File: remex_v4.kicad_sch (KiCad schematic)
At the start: 22 parts, among them J1 Conn_01x03_Male, J10 Conn_01x04_Male, J11 Conn_01x04_Male, J2 Conn_01x03_Male, J3 Conn_01x06_Male, J4 Conn_01x04_Male, J5 Conn_01x02_Male, J6 Conn_01x03_Male, J7 Conn_01x02_Male, J8 Conn_01x03_Male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

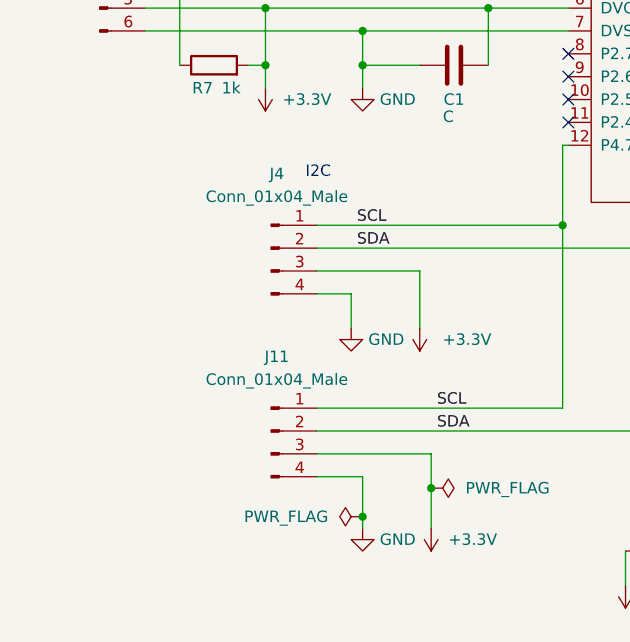
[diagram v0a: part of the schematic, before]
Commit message: Corrected qwiic orientation, added silkscreen details, changed diodes to 0805, fixed bugs with qei
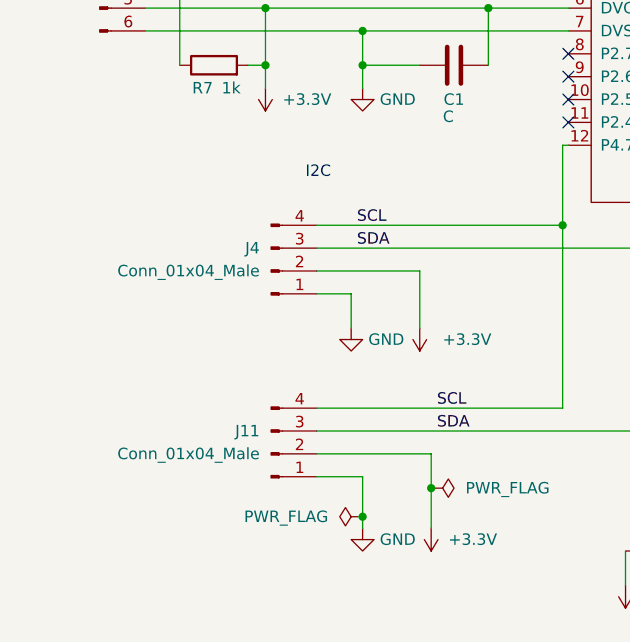
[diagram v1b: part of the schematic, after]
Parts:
- D1, D2: footprint LED_SMD:LED_0603_1608Metric_Pad1.05x0.95mm_HandSolder -> LED_SMD:LED_0805_2012Metric
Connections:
- net +3.3V: now also J11.2 (Pin_2), J4.2 (Pin_2); no longer J11.3 (Pin_3), J4.3 (Pin_3)
- net GND: now also J11.1 (Pin_1), J4.1 (Pin_1); no longer J11.4 (Pin_4), J4.4 (Pin_4)
- net SCL: now also J11.4 (Pin_4), J4.4 (Pin_4); no longer J11.1 (Pin_1), J4.1 (Pin_1)
- net SDA: now also J11.3 (Pin_3), J4.3 (Pin_3); no longer J11.2 (Pin_2), J4.2 (Pin_2)
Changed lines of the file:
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@@
     (title "Remex")
     (date "2023-01-23")
-    (rev "v4.0.0")
+    (rev "v4.0.1")
     (company "Montana Tech Robotics Club")
     (comment 1 "Author: Justin Bak")
@@
     (property "Reference" "D2" (id 0) (at 119.6975 130.175 0))
     (property "Value" "LED" (id 1) (at 119.6975 132.715 0))
-    (property "Footprint" "LED_SMD:LED_0603_1608Metric_Pad1.05x0.95mm_HandSolder" (id 2) (at 118.11 137.16 0)
+    (property "Footprint" "LED_SMD:LED_0805_2012Metric" (id 2) (at 118.11 137.16 0)
       (effects (font (size 1.27 1.27)) hide)
     )
@@
     (pin "1")
   )
-  (symbol (lib_id "Connector:Conn_01x04_Male") (at 74.93 123.825 0) (unit 1)
-    (in_bom yes) (on_board yes) (fields_autoplaced)
-    (property "Reference" "J11" (id 0) (at 75.565 115.57 0))
-    (property "Value" "Conn_01x04_Male" (id 1) (at 75.565 118.11 0))
-    (property "Footprint" "Connector_JST:JST_SH_SM04B-SRSS-TB_1x04-1MP_P1.00mm_Horizontal" (id 2) (at 74.93 123.825 0)
-      (effects (font (size 1.27 1.27)) hide)
-    )
-    (property "Datasheet" "~" (id 3) (at 74.93 123.825 0)
+  (symbol (lib_id "Connector:Conn_01x04_Male") (at 74.93 126.365 0) (mirror x) (unit 1)
+    (in_bom yes) (on_board yes) (fields_autoplaced)
+    (property "Reference" "J11" (id 0) (at 73.66 123.8249 0)
+      (effects (font (size 1.27 1.27)) (justify right))
+    )
+    (property "Value" "Conn_01x04_Male" (id 1) (at 73.66 126.3649 0)
+      (effects (font (size 1.27 1.27)) (justify right))
+    )
+    (property "Footprint" "Connector_JST:JST_SH_SM04B-SRSS-TB_1x04-1MP_P1.00mm_Horizontal" (id 2) (at 74.93 126.365 0)
+      (effects (font (size 1.27 1.27)) hide)
+    )
+    (property "Datasheet" "~" (id 3) (at 74.93 126.365 0)
       (effects (font (size 1.27 1.27)) hide)
     )
@@
     (property "Reference" "D1" (id 0) (at 146.685 50.165 0))
     (property "Value" "LED" (id 1) (at 149.86 50.165 0))
-    (property "Footprint" "LED_SMD:LED_0603_1608Metric_Pad1.05x0.95mm_HandSolder" (id 2) (at 150.495 52.705 0)
+    (property "Footprint" "LED_SMD:LED_0805_2012Metric" (id 2) (at 150.495 52.705 0)
       (effects (font (size 1.27 1.27)) hide)
     )
@@
     (pin "2")
   )
-  (symbol (lib_id "Connector:Conn_01x04_Male") (at 74.93 103.505 0) (unit 1)
-    (in_bom yes) (on_board yes) (fields_autoplaced)
-    (property "Reference" "J4" (id 0) (at 75.565 95.25 0))
-    (property "Value" "Conn_01x04_Male" (id 1) (at 75.565 97.79 0))
-    (property "Footprint" "Connector_JST:JST_SH_SM04B-SRSS-TB_1x04-1MP_P1.00mm_Horizontal" (id 2) (at 74.93 103.505 0)
-      (effects (font (size 1.27 1.27)) hide)
-    )
-    (property "Datasheet" "~" (id 3) (at 74.93 103.505 0)
+  (symbol (lib_id "Connector:Conn_01x04_Male") (at 74.93 106.045 0) (mirror x) (unit 1)
+    (in_bom yes) (on_board yes) (fields_autoplaced)
+    (property "Reference" "J4" (id 0) (at 73.66 103.5049 0)
+      (effects (font (size 1.27 1.27)) (justify right))
+    )
+    (property "Value" "Conn_01x04_Male" (id 1) (at 73.66 106.0449 0)
+      (effects (font (size 1.27 1.27)) (justify right))
+    )
+    (property "Footprint" "Connector_JST:JST_SH_SM04B-SRSS-TB_1x04-1MP_P1.00mm_Horizontal" (id 2) (at 74.93 106.045 0)
+      (effects (font (size 1.27 1.27)) hide)
+    )
+    (property "Datasheet" "~" (id 3) (at 74.93 106.045 0)
       (effects (font (size 1.27 1.27)) hide)
     )
@@
     )
     (path "/f2f40641-9cde-42a3-b33f-7fc15e3c41ff"
-      (reference "D1") (unit 1) (value "LED") (footprint "LED_SMD:LED_0603_1608Metric_Pad1.05x0.95mm_HandSolder")
+      (reference "D1") (unit 1) (value "LED") (footprint "LED_SMD:LED_0805_2012Metric")
     )
     (path "/d0d29197-3e4c-49b8-a4d7-e06c8e60fb9a"
-      (reference "D2") (unit 1) (value "LED") (footprint "LED_SMD:LED_0603_1608Metric_Pad1.05x0.95mm_HandSolder")
+      (reference "D2") (unit 1) (value "LED") (footprint "LED_SMD:LED_0805_2012Metric")
     )
     (path "/81b7d991-97ff-4f77-8d76-10511c91fd8c"
